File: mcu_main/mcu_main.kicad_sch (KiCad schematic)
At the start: 19 parts, among them J10 Conn_01x02_Pin, J2 Conn_01x10_Pin, J3 Conn_01x06_Pin, U1 ESP32-S3-WROOM-1, U3 SGM2212-3.3, sw1 SW_Push_Dual, sw2 SW_Push_Dual

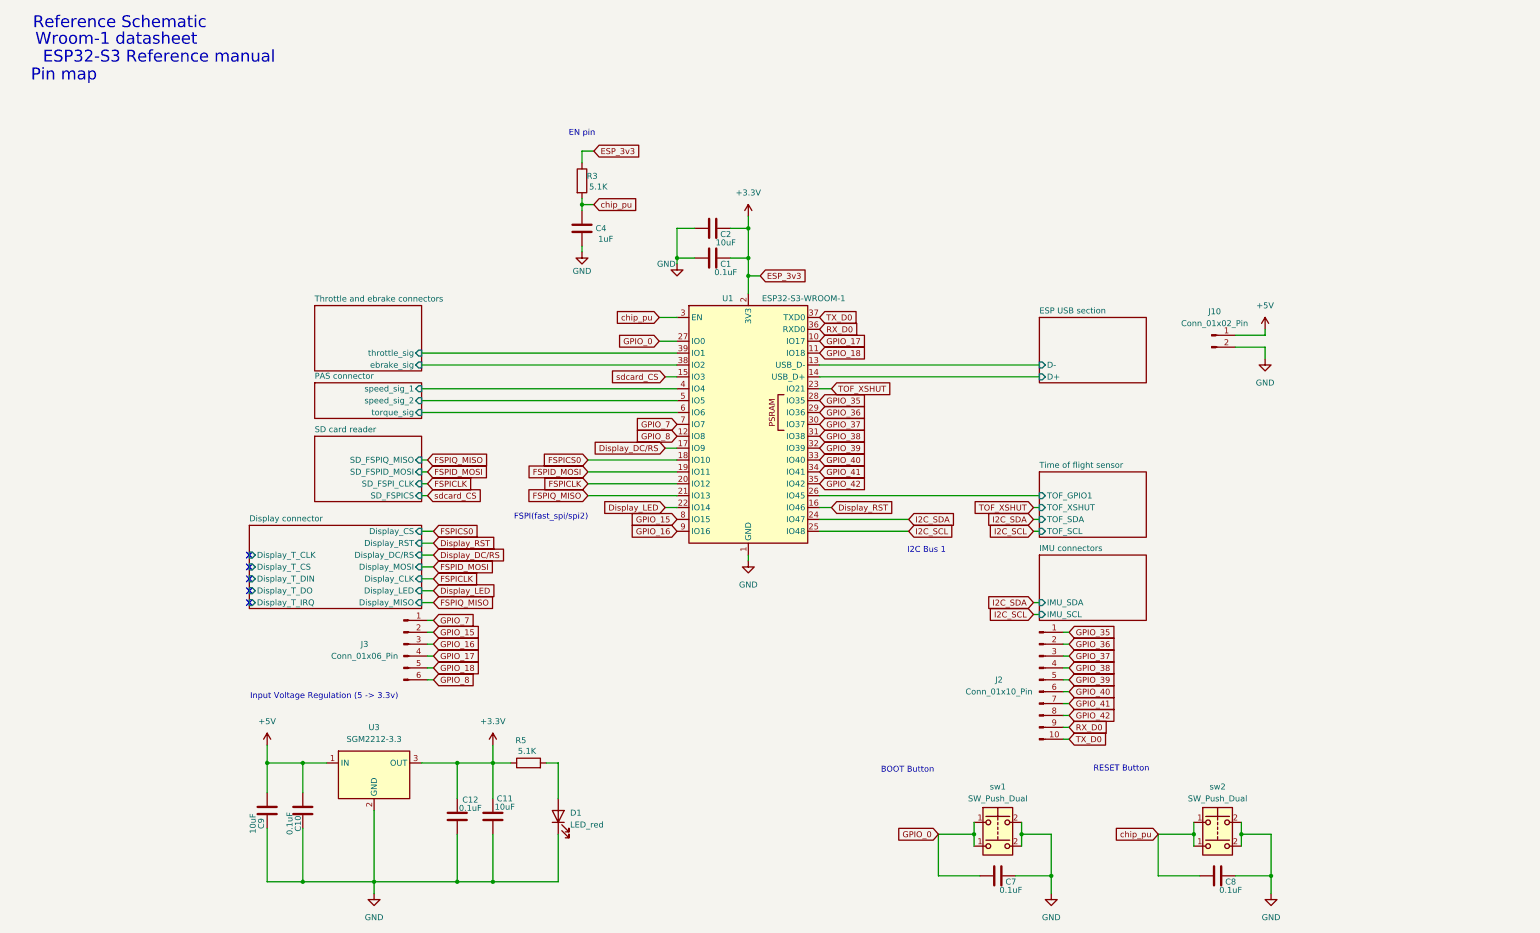
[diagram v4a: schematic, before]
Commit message: test points and silkscreen annotations
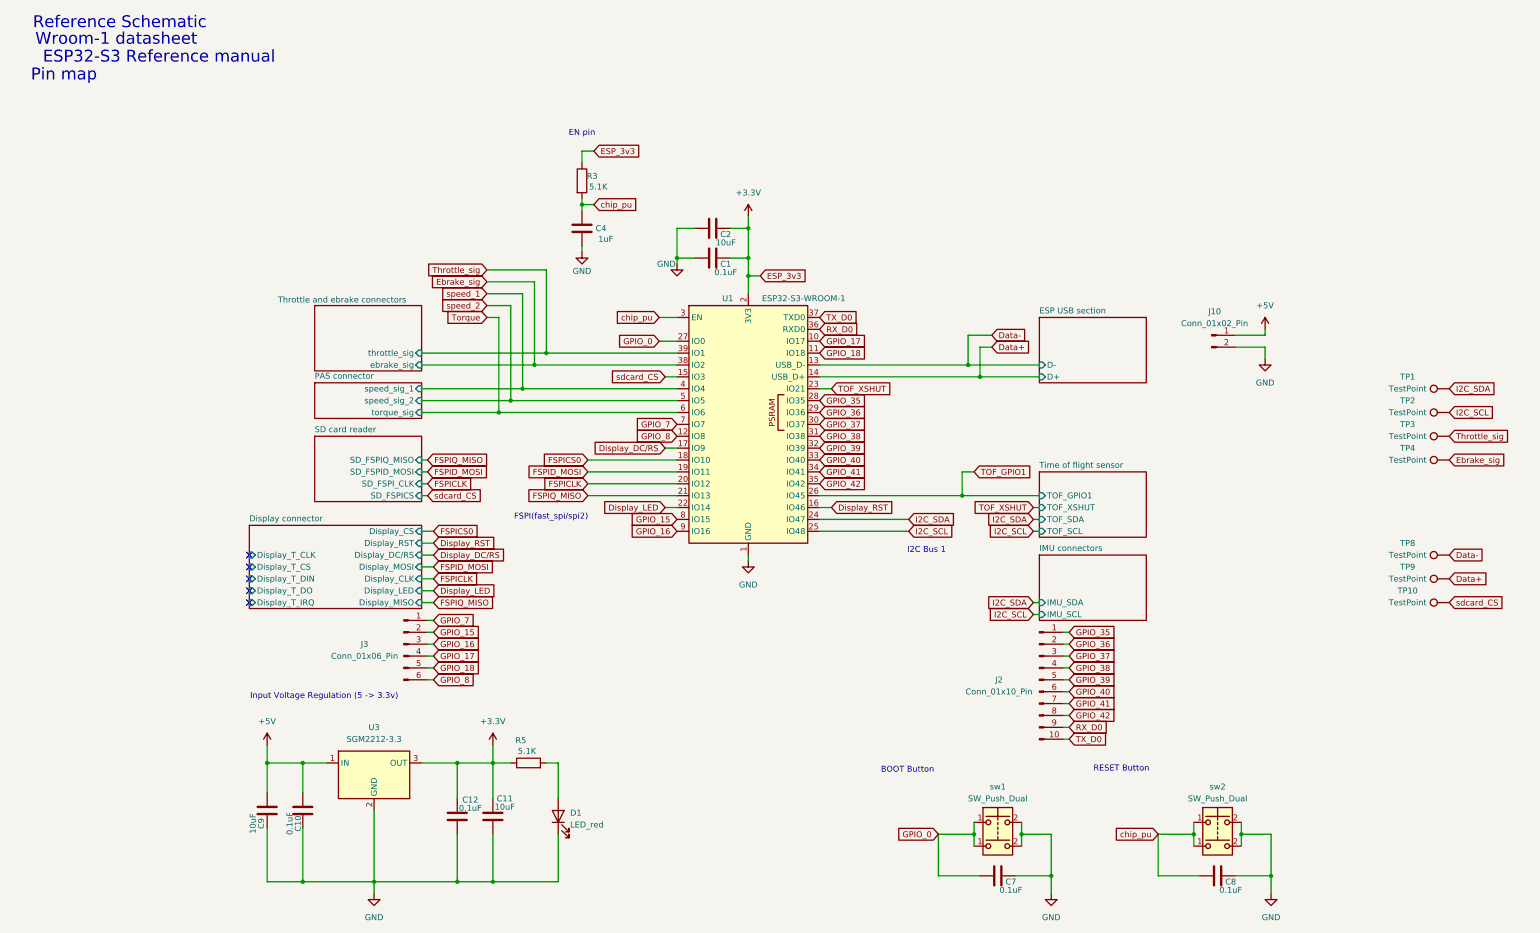
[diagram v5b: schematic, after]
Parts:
- added TP1, TP10, TP2, TP3, TP4, TP8, TP9: TestPoint, TestPoint:TestPoint_Pad_2.0x2.0mm, symbol Connector:TestPoint
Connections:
- net I2C_SCL: now also TP2.1
- net I2C_SDA: now also TP1.1
- net sdcard_CS: now also TP10.1
- net ESP USB section/D+ renamed Data+
- net Data+: now also TP9.1
- net ESP USB section/D- renamed Data-
- net Data-: now also TP8.1
- net PAS connector/speed_sig_1 renamed speed_1
- net PAS connector/speed_sig_2 renamed speed_2
- net PAS connector/torque_sig renamed Torque
- net Throttle and ebrake connectors/ebrake_sig renamed Ebrake_sig
- net Ebrake_sig: now also TP4.1
- net Throttle and ebrake connectors/throttle_sig renamed Throttle_sig
- net Throttle_sig: now also TP3.1
- net Time of flight sensor/TOF_GPIO1 renamed TOF_GPIO1
